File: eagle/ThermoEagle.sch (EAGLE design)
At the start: 35 parts, among them IC1 MAX232, IC2 4511N, Q1 20MHz, T1 2N2219, T2 2N2219, U1 LM324

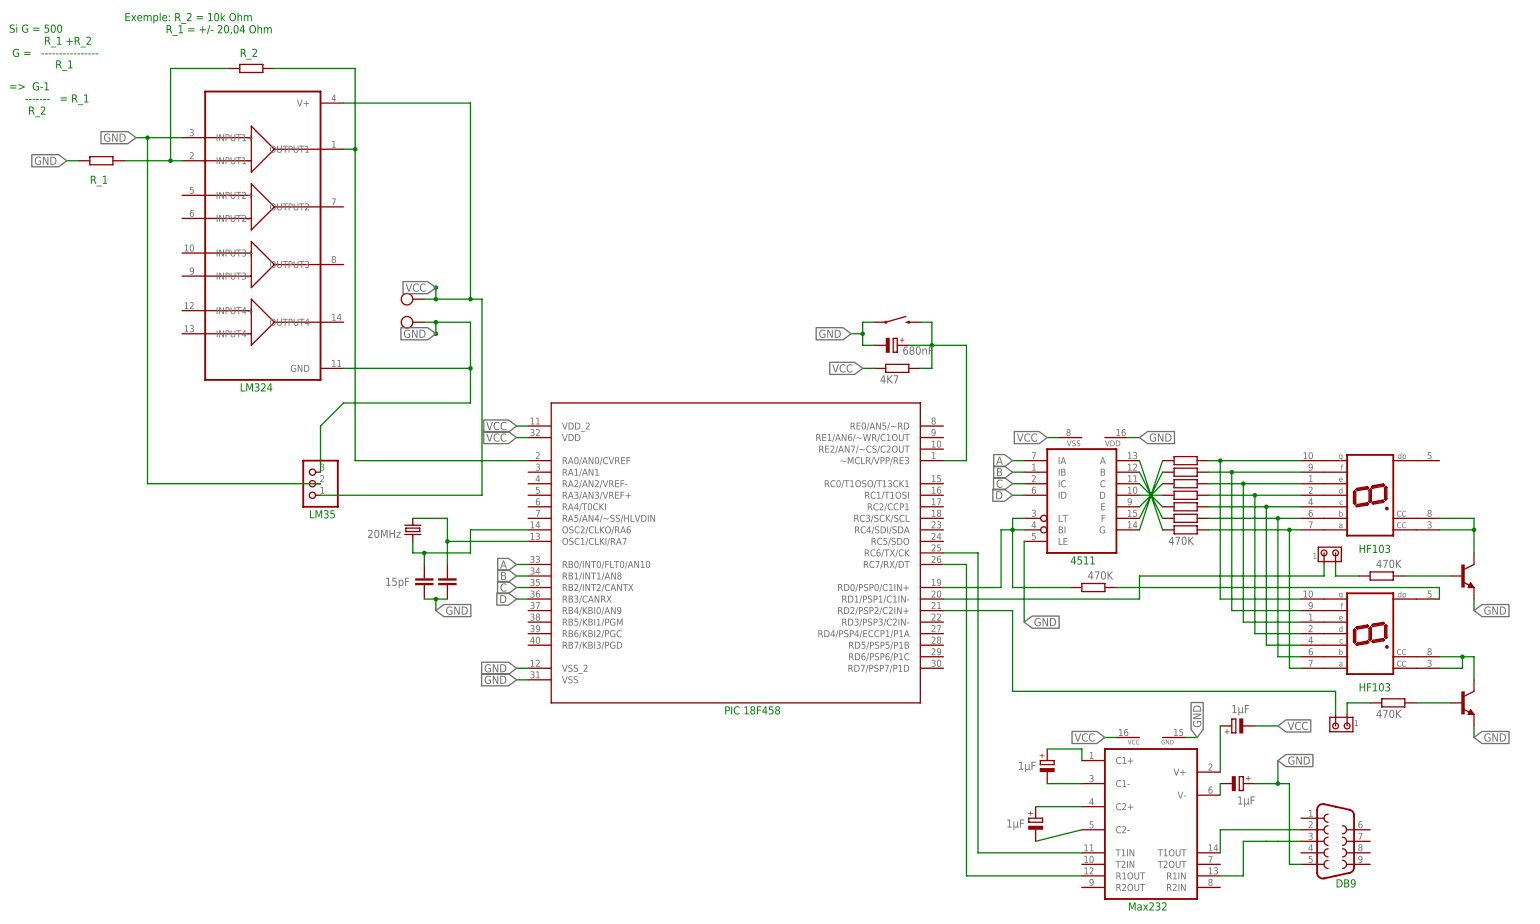
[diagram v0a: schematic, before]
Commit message: changement du schéma eagle et proteus
dernier ajout ou changement du montage
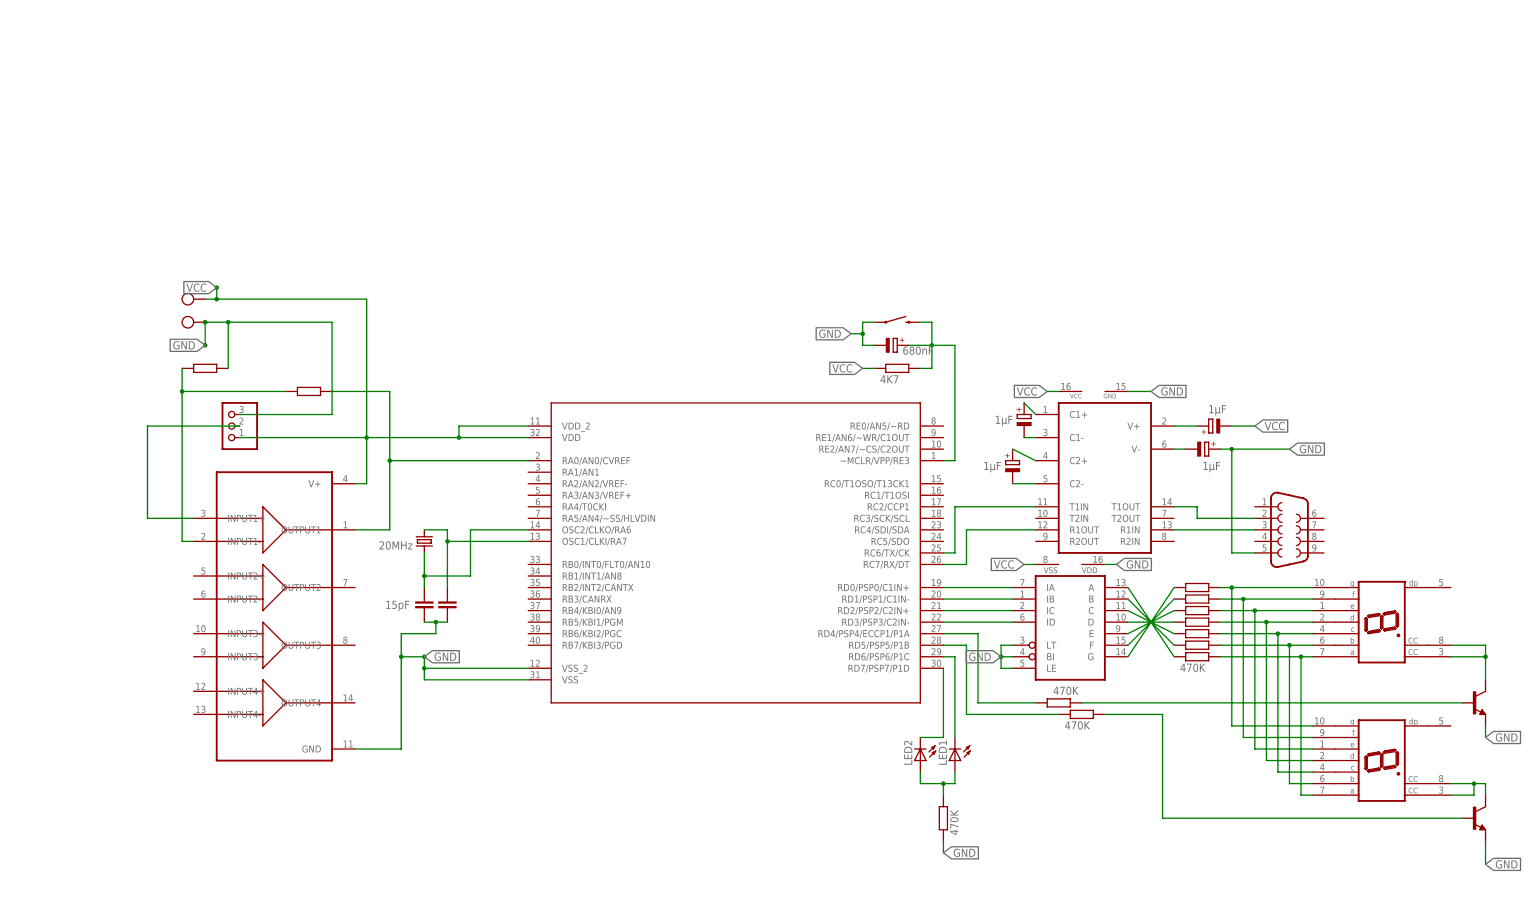
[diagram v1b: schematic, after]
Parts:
- removed J2, J3: (no value), con-amp:MTA02-156
- removed R9: 470K, resistor:R-EU_0207/7
- added LED1, LED2: (no value), eagle-ltspice:LED_ELD260
- added R1: 470K, resistor:R-EU_0207/7
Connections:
- removed net A: U$1.RB0/INT0/FLT0/AN10
- removed net B: U$1.RB1/INT1/AN8
- removed net C: U$1.RB2/INT2/CANTX
- removed net D: U$1.RB3/CANRX
- removed net N$2 (its old number): J2.2, U$1.RD2/PSP2/C2IN+
- removed net N$47: U$1.VSS
- removed net N$51: R13.1
- removed net N$54: C6.2, C7.2
- removed net N$58: IC2A.IB
- removed net N$59: IC2A.IC
- removed net N$60: IC2A.ID
- new net N$23: LED1.A, LED2.A, R1.2
- net GND: now also C6.2, C7.2, R13.1, U$1.VSS, U$1.VSS_2
- net N$1: now also IC2A.IA, U$1.RD0/PSP0/C1IN+; no longer DIS2.DP, R9.2
- net N$11: now also IC2A.IC, U$1.RD2/PSP2/C2IN+; no longer IC2A.BI, IC2A.LT, R9.1, U$1.RD0/PSP0/C1IN+
- net N$22: now also IC2A.ID, U$1.RD3/PSP3/C2IN-; no longer IC2A.IA
- net N$37: now also LED2.C, U$1.RD7/PSP7/P1D; no longer J3.2, R10.1
- net N$38: now also R10.1, U$1.RD4/PSP4/ECCP1/P1A; no longer J2.1, R11.1
- net N$44: now also R11.1, U$1.RD5/PSP5/P1B; no longer U$1.VDD_2
- net N$45: now also LED1.C, U$1.RD6/PSP6/P1C; no longer U$1.VDD
- net N$46: now also R1.1; no longer U$1.VSS_2
- net N$5: now also IC2A.BI, IC2A.LE, IC2A.LT; no longer J3.1, U$1.RD1/PSP1/C1IN-
- net N$6: now also IC2A.IB, U$1.RD1/PSP1/C1IN-; no longer IC2A.LE
- net VCC: now also U$1.VDD, U$1.VDD_2
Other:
- note removed: "4511"
- note removed: "=> G-1 ------- = R_1 R_2"
- note removed: "DB9"
- note removed: "Exemple: R_2 = 10k Ohm R_1 = +/- 20,04 Ohm"
- note removed: "HF103"
- note removed: "LM324"
- note removed: "LM35"
- note removed: "Max232"
- note removed: "PIC 18F458"
- note removed: "R_1"
- note removed: "R_2"
- note removed: "Si G = 500 R_1 +R_2 G = ----------------"

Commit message: Eagle to fix by Maxime
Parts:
- removed J1: (no value), SparkFun-Connectors:DB9FEMALE
- removed R_2: (no value), resistor:R-EU_0207/7
- added J2: (no value), con-amp:MTA03-100
- added X2: (no value), con-subd:F09VB
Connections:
- net N$2: no longer J1.2
- net N$20: no longer J1.5
- net N$21: no longer J1.3
- net N$49: no longer R_2.2
- net N$50: no longer R_2.1
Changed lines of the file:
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@@
 <part name="U$1" library="PIC18F4585-I_P" deviceset="PIC18F4585-I/P" device=""/>
 <part name="IC1" library="maxim" library_urn="urn:adsk.eagle:library:269" deviceset="MAX232" device="" package3d_urn="urn:adsk.eagle:package:922/2"/>
-<part name="J1" library="SparkFun-Connectors" library_urn="urn:adsk.eagle:library:513" deviceset="DB9" device="FEMALE" package3d_urn="urn:adsk.eagle:package:38025/1"/>
 <part name="IC2" library="45xx" library_urn="urn:adsk.eagle:library:82" deviceset="4511" device="N" package3d_urn="urn:adsk.eagle:package:922/2"/>
 <part name="DIS1" library="display-hp" library_urn="urn:adsk.eagle:library:212" deviceset="HD-H103" device="" package3d_urn="urn:adsk.eagle:package:13006/1"/>
@@
 <part name="JP1" library="adafruit" library_urn="urn:adsk.eagle:library:420" deviceset="PINHD-1X3" device="" package3d_urn="urn:adsk.eagle:package:6240710/1"/>
 <part name="U1" library="LM324" deviceset="LM324" device=""/>
-<part name="R_2" library="resistor" library_urn="urn:adsk.eagle:library:348" deviceset="R-EU_" device="0207/7" package3d_urn="urn:adsk.eagle:package:23493/2"/>
 <part name="R13" library="resistor" library_urn="urn:adsk.eagle:library:348" deviceset="R-EU_" device="0207/7" package3d_urn="urn:adsk.eagle:package:23493/2"/>
 <part name="X1" library="con-ptr500" library_urn="urn:adsk.eagle:library:181" deviceset="AK300/2" device="" package3d_urn="urn:adsk.eagle:package:9881/1"/>
@@
 <part name="LED2" library="eagle-ltspice" library_urn="urn:adsk.eagle:library:217" deviceset="LED_E" device="LD260" package3d_urn="urn:adsk.eagle:package:13313/1"/>
 <part name="R1" library="resistor" library_urn="urn:adsk.eagle:library:348" deviceset="R-EU_" device="0207/7" package3d_urn="urn:adsk.eagle:package:23493/2" value="470K"/>
+<part name="J2" library="con-amp" library_urn="urn:adsk.eagle:library:127" deviceset="MTA03-100" device="" package3d_urn="urn:adsk.eagle:package:8081621/1"/>
+<part name="X2" library="con-subd" library_urn="urn:adsk.eagle:library:189" deviceset="F09" device="VB" package3d_urn="urn:adsk.eagle:package:10282/1"/>
 </parts>
 <sheets>
@@
 <instance part="U$1" gate="A" x="-35.56" y="73.66" smashed="yes"/>
 <instance part="IC1" gate="G$1" x="45.72" y="88.9" smashed="yes"/>
-<instance part="J1" gate="G$1" x="86.36" y="76.2" smashed="yes">
-<attribute name="VALUE" x="82.55" y="67.818" size="1.778" layer="96" font="vector" align="top-left"/>
-</instance>
 <instance part="IC2" gate="A" x="38.1" y="55.88" smashed="yes"/>
 <instance part="DIS1" gate="N" x="106.68" y="55.88" smashed="yes" rot="MR270"/>
@@
 </instance>
 <instance part="U1" gate="A" x="-137.16" y="58.42" smashed="yes"/>
-<instance part="R_2" gate="G$1" x="-129.54" y="106.68" smashed="yes">
-<attribute name="VALUE" x="-133.35" y="103.378" size="1.778" layer="96"/>
-</instance>
 <instance part="R13" gate="G$1" x="-152.4" y="111.76" smashed="yes" rot="R180">
 <attribute name="VALUE" x="-148.59" y="115.062" size="1.778" layer="96" rot="R180"/>
@@
 <instance part="R1" gate="G$1" x="10.16" y="12.7" smashed="yes" rot="R90">
 <attribute name="VALUE" x="13.462" y="8.89" size="1.778" layer="96" rot="R90"/>
+</instance>
+<instance part="J2" gate="G$1" x="-129.54" y="106.68" smashed="yes">
+<attribute name="NAME" x="-124.46" y="106.68" size="1.778" layer="95"/>
+<attribute name="VALUE" x="-124.46" y="102.87" size="1.778" layer="96"/>
+</instance>
+<instance part="X2" gate="G$1" x="88.9" y="76.2" smashed="yes">
+<attribute name="VALUE" x="85.09" y="65.405" size="1.778" layer="96"/>
+<attribute name="NAME" x="85.09" y="85.09" size="1.778" layer="95"/>
 </instance>
 </instances>
@@
 <net name="N$21" class="0">
 <segment>
-<pinref part="J1" gate="G$1" pin="3"/>
 <pinref part="IC1" gate="G$1" pin="R1IN"/>
 <wire x1="60.96" y1="76.2" x2="78.74" y2="76.2" width="0.1524" layer="91"/>
@@
 <segment>
 <wire x1="73.66" y1="93.98" x2="73.66" y2="71.12" width="0.1524" layer="91"/>
-<pinref part="J1" gate="G$1" pin="5"/>
 <wire x1="73.66" y1="71.12" x2="78.74" y2="71.12" width="0.1524" layer="91"/>
 <pinref part="C3" gate="G$1" pin="+"/>
@@
 <wire x1="-111.76" y1="106.68" x2="-111.76" y2="91.44" width="0.1524" layer="91"/>
 <wire x1="-124.46" y1="106.68" x2="-111.76" y2="106.68" width="0.1524" layer="91"/>
-<pinref part="R_2" gate="G$1" pin="2"/>
 <pinref part="U$1" gate="A" pin="RA0/AN0/CVREF"/>
 <wire x1="-81.28" y1="91.44" x2="-111.76" y2="91.44" width="0.1524" layer="91"/>
@@
 <segment>
 <wire x1="-157.48" y1="106.68" x2="-134.62" y2="106.68" width="0.1524" layer="91"/>
-<pinref part="R_2" gate="G$1" pin="1"/>
 <pinref part="R13" gate="G$1" pin="2"/>
 <wire x1="-157.48" y1="106.68" x2="-157.48" y2="111.76" width="0.1524" layer="91"/>
@@
 <net name="N$2" class="0">
 <segment>
-<pinref part="J1" gate="G$1" pin="2"/>
 <pinref part="IC1" gate="G$1" pin="T1OUT"/>
 <wire x1="60.96" y1="81.28" x2="66.04" y2="81.28" width="0.1524" layer="91"/>
